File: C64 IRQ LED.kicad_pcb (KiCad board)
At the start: 2 copper layers, 38.7 x 12.7 mm, 6 parts, among them J1 Signals, J2 ENABLE, U1 74LS04

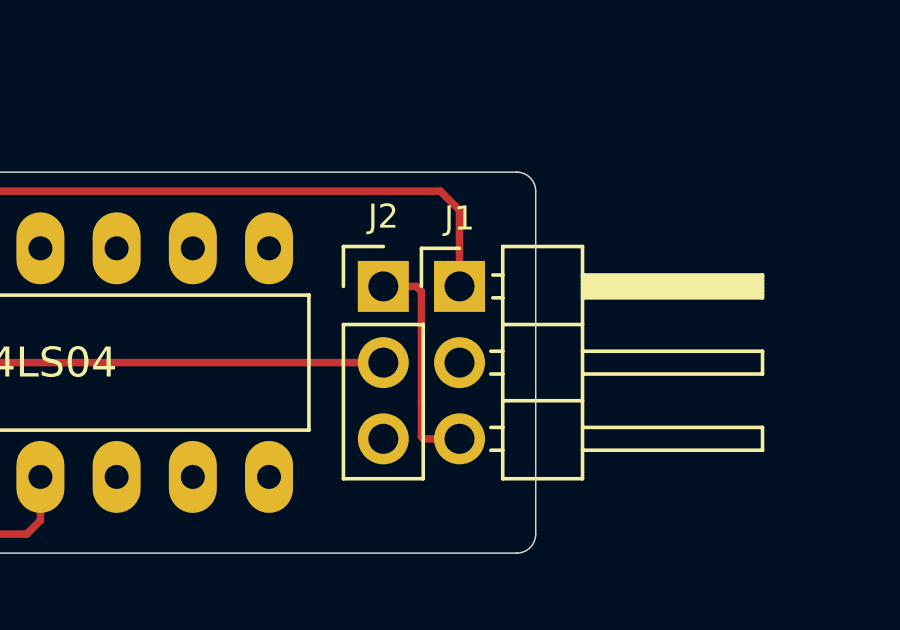
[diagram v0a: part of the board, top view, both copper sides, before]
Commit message: Changed pin order to match expansion port
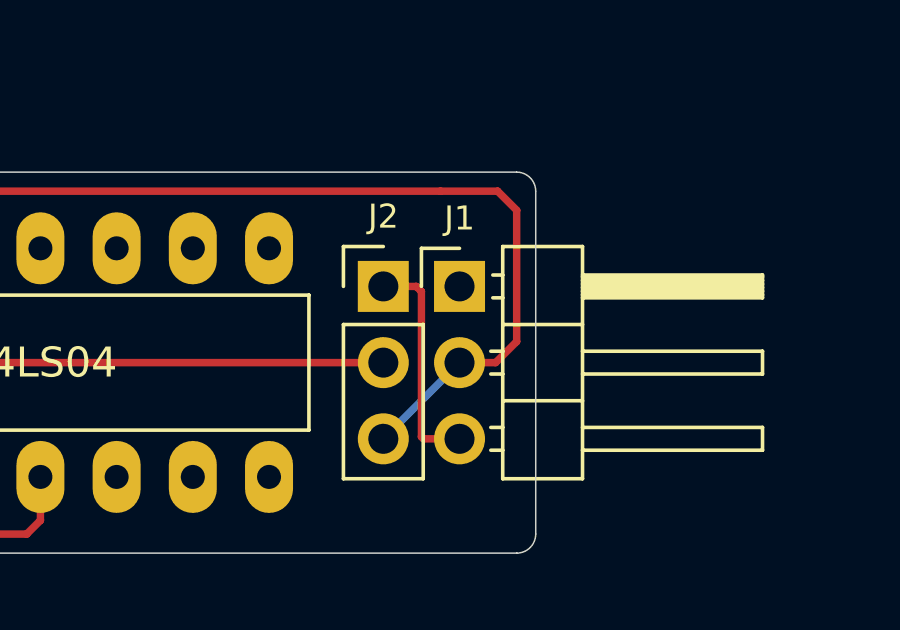
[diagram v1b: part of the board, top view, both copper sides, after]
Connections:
- J1 pad 1: VCC -> GND
- J1 pad 2: GND -> VCC
- J2 pad 3: GND -> VCC
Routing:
- net VCC: track 26.0 -> 35.6 mm
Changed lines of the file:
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@@
     (thickness 1.6)
     (drawings 34)
-    (tracks 36)
+    (tracks 40)
     (zones 0)
     (modules 6)
@@
   (page A4)
   (layers
-    (0 F.Cu signal)
-    (31 B.Cu signal)
+    (0 F.Cu signal hide)
+    (31 B.Cu signal hide)
     (32 B.Adhes user)
     (33 F.Adhes user)
@@
       (net 4 "Net-(J1-Pad3)"))
     (pad 2 thru_hole oval (at 0 2.54) (size 1.7 1.7) (drill 1) (layers *.Cu *.Mask)
-      (net 2 GND))
+      (net 5 VCC))
     (pad 1 thru_hole rect (at 0 0) (size 1.7 1.7) (drill 1) (layers *.Cu *.Mask)
-      (net 5 VCC))
+      (net 2 GND))
     (model ${KISYS3DMOD}/Pin_Headers.3dshapes/Pin_Header_Angled_1x03_Pitch2.54mm.wrl
       (at (xyz 0 0 0))
@@
     (fp_line (start -0.635 -1.27) (end 1.27 -1.27) (layer F.Fab) (width 0.1))
     (pad 3 thru_hole oval (at 0 5.08) (size 1.7 1.7) (drill 1) (layers *.Cu *.Mask)
-      (net 2 GND))
+      (net 5 VCC))
     (pad 2 thru_hole oval (at 0 2.54) (size 1.7 1.7) (drill 1) (layers *.Cu *.Mask)
       (net 8 "Net-(J2-Pad2)"))
@@
     (effects (font (size 0.8 0.8) (thickness 0.1)) (justify mirror))
   )
-  (gr_text GND (at 150.495 114.935 90) (layer B.SilkS)
-    (effects (font (size 0.8 0.8) (thickness 0.1)) (justify mirror))
-  )
-  (gr_text VCC (at 150.495 112.395 90) (layer B.SilkS)
+  (gr_text GND (at 150.495 112.395 90) (layer B.SilkS)
+    (effects (font (size 0.8 0.8) (thickness 0.1)) (justify mirror))
+  )
+  (gr_text VCC (at 150.495 114.935 90) (layer B.SilkS)
     (effects (font (size 0.8 0.8) (thickness 0.1)) (justify mirror))
   )
@@
   (gr_line (start 151.13 109.22) (end 151.13 120.65) (layer Edge.Cuts) (width 0.05))
   (gr_line (start 113.03 108.585) (end 150.495 108.585) (layer Edge.Cuts) (width 0.05))
-  (segment (start 116.205 114.935) (end 114.3 114.935) (width 0.25) (layer F.Cu) (net 1))
-  (segment (start 113.665 114.3) (end 113.665 109.855) (width 0.25) (layer F.Cu) (net 1))
+  (segment (start 116.205 114.935) (end 114.3 114.935) (width 0.25) (layer F.Cu) (net 1) (status 10))
+  (segment (start 113.665 114.3) (end 113.665 109.855) (width 0.25) (layer F.Cu) (net 1) (status 20))
   (segment (start 114.3 114.935) (end 113.665 114.3) (width 0.25) (layer F.Cu) (net 1))
   (segment (start 121.285 116.085) (end 120.65 116.72) (width 0.25) (layer F.Cu) (net 3))
-  (segment (start 121.285 114.935) (end 121.285 116.085) (width 0.25) (layer F.Cu) (net 3))
+  (segment (start 121.285 114.935) (end 121.285 116.085) (width 0.25) (layer F.Cu) (net 3) (status 10))
   (segment (start 120.65 116.72) (end 114.42 116.72) (width 0.25) (layer F.Cu) (net 3))
-  (segment (start 113.665 117.475) (end 113.665 120.015) (width 0.25) (layer F.Cu) (net 3))
+  (segment (start 113.665 117.475) (end 113.665 120.015) (width 0.25) (layer F.Cu) (net 3) (status 20))
   (segment (start 114.42 116.72) (end 113.665 117.475) (width 0.25) (layer F.Cu) (net 3))
   (segment (start 147.15 112.395) (end 147.32 112.565) (width 0.25) (layer F.Cu) (net 4))
-  (segment (start 146.05 112.395) (end 147.15 112.395) (width 0.25) (layer F.Cu) (net 4))
+  (segment (start 146.05 112.395) (end 147.15 112.395) (width 0.25) (layer F.Cu) (net 4) (status 10))
   (segment (start 147.32 112.565) (end 147.32 116.205) (width 0.25) (layer F.Cu) (net 4))
   (segment (start 147.387919 117.475) (end 147.32 117.407081) (width 0.25) (layer F.Cu) (net 4))
-  (segment (start 148.59 117.475) (end 147.387919 117.475) (width 0.25) (layer F.Cu) (net 4))
+  (segment (start 148.59 117.475) (end 147.387919 117.475) (width 0.25) (layer F.Cu) (net 4) (status 10))
   (segment (start 147.32 117.407081) (end 147.32 116.205) (width 0.25) (layer F.Cu) (net 4))
   (segment (start 127 109.675) (end 127.455 109.22) (width 0.25) (layer F.Cu) (net 5))
-  (segment (start 127 111.125) (end 127 109.675) (width 0.25) (layer F.Cu) (net 5))
+  (segment (start 127 111.125) (end 127 109.675) (width 0.25) (layer F.Cu) (net 5) (status 10))
   (segment (start 127.455 109.22) (end 147.955 109.22) (width 0.25) (layer F.Cu) (net 5))
-  (segment (start 148.59 109.855) (end 148.59 112.395) (width 0.25) (layer F.Cu) (net 5))
-  (segment (start 147.955 109.22) (end 148.59 109.855) (width 0.25) (layer F.Cu) (net 5))
-  (segment (start 123.825 120.015) (end 124.46 120.65) (width 0.25) (layer F.Cu) (net 6))
-  (segment (start 134.62 120.195) (end 134.62 118.745) (width 0.25) (layer F.Cu) (net 6))
+  (segment (start 146.05 117.475) (end 148.59 114.935) (width 0.25) (layer B.Cu) (net 5))
+  (segment (start 149.792081 114.935) (end 150.495 114.232081) (width 0.25) (layer F.Cu) (net 5))
+  (segment (start 148.59 114.935) (end 149.792081 114.935) (width 0.25) (layer F.Cu) (net 5))
+  (segment (start 150.495 114.232081) (end 150.495 109.855) (width 0.25) (layer F.Cu) (net 5))
+  (segment (start 149.86 109.22) (end 147.955 109.22) (width 0.25) (layer F.Cu) (net 5))
+  (segment (start 150.495 109.855) (end 149.86 109.22) (width 0.25) (layer F.Cu) (net 5))
+  (segment (start 123.825 120.015) (end 124.46 120.65) (width 0.25) (layer F.Cu) (net 6) (status 10))
+  (segment (start 134.62 120.195) (end 134.62 118.745) (width 0.25) (layer F.Cu) (net 6) (status 20))
   (segment (start 134.165 120.65) (end 134.62 120.195) (width 0.25) (layer F.Cu) (net 6))
   (segment (start 124.46 120.65) (end 134.165 120.65) (width 0.25) (layer F.Cu) (net 6))
-  (segment (start 129.54 118.745) (end 132.08 118.745) (width 0.25) (layer F.Cu) (net 7))
-  (segment (start 123.825 109.855) (end 123.825 115.57) (width 0.25) (layer F.Cu) (net 7))
+  (segment (start 129.54 118.745) (end 132.08 118.745) (width 0.25) (layer F.Cu) (net 7) (status 30))
+  (segment (start 123.825 109.855) (end 123.825 115.57) (width 0.25) (layer F.Cu) (net 7) (status 10))
   (via (at 125.73 116.205) (size 0.8) (drill 0.4) (layers F.Cu B.Cu) (net 7))
   (segment (start 123.825 115.57) (end 124.46 116.205) (width 0.25) (layer F.Cu) (net 7))
@@
   (segment (start 125.73 116.205) (end 128.27 116.205) (width 0.25) (layer B.Cu) (net 7))
   (segment (start 128.27 116.205) (end 128.905 116.205) (width 0.25) (layer F.Cu) (net 7))
-  (segment (start 129.54 116.84) (end 129.54 118.745) (width 0.25) (layer F.Cu) (net 7))
+  (segment (start 129.54 116.84) (end 129.54 118.745) (width 0.25) (layer F.Cu) (net 7) (status 20))
   (segment (start 128.905 116.205) (end 129.54 116.84) (width 0.25) (layer F.Cu) (net 7))
-  (segment (start 146.05 114.935) (end 127.635 114.935) (width 0.25) (layer F.Cu) (net 8))
-  (segment (start 127 115.57) (end 127 118.745) (width 0.25) (layer F.Cu) (net 8))
+  (segment (start 146.05 114.935) (end 127.635 114.935) (width 0.25) (layer F.Cu) (net 8) (status 10))
+  (segment (start 127 115.57) (end 127 118.745) (width 0.25) (layer F.Cu) (net 8) (status 20))
   (segment (start 127.635 114.935) (end 127 115.57) (width 0.25) (layer F.Cu) (net 8))
   (zone (net 2) (net_name GND) (layer B.Cu) (hatch edge 0.508)
